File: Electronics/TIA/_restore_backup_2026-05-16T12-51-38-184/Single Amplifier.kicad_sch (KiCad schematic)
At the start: 3 parts, among them U1 ${SIM.PARAMS}

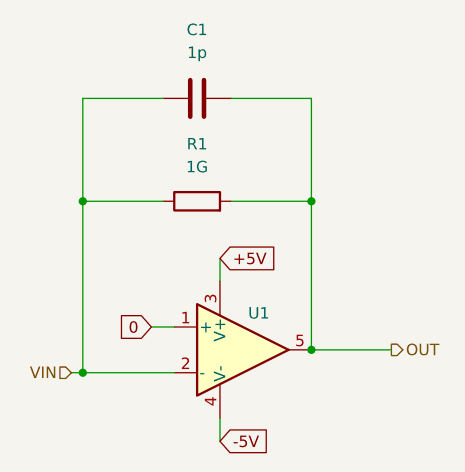
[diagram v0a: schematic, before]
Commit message: Create a robust TIA design following the requirements
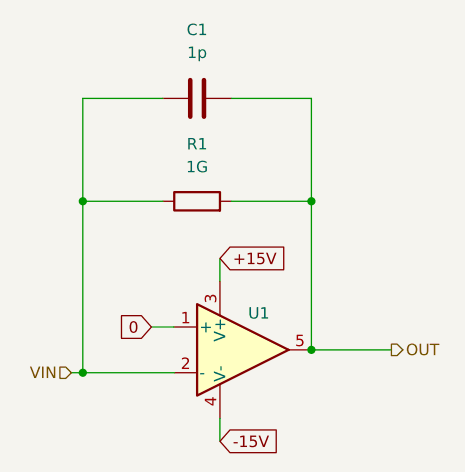
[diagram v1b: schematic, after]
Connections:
- net +5V renamed +15V
- net -5V renamed -15V
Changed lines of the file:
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@@
 		)
 	)
-	(global_label "-5V"
+	(global_label "-15V"
 		(shape input)
 		(at 144.78 118.11 0)
@@
 		)
 		(property "Intersheetrefs" "${INTERSHEET_REFS}"
-			(at 151.6357 118.11 0)
+			(at 152.8452 118.11 0)
 			(hide yes)
 			(show_name no)
@@
 		)
 	)
-	(global_label "+5V"
+	(global_label "+15V"
 		(shape input)
 		(at 144.78 97.79 0)
@@
 		)
 		(property "Intersheetrefs" "${INTERSHEET_REFS}"
-			(at 151.6357 97.79 0)
+			(at 152.8452 97.79 0)
 			(hide yes)
 			(show_name no)
